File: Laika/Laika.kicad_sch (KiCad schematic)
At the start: 0 parts

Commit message: Defined Hierarchal Sheet Layout
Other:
- added sheet Project Architecture (sheets/ProjectArchitecture.kicad_sch)
- note added: "${BOARD_NAME}"
- note added: "${RELEASE_DATE}"
- note added: "1"
- note added: "10"
- note added: "11"
- note added: "12"
- note added: "13"
- note added: "14"
- note added: "15"
- note added: "2"
- note added: "3"
- note added: "4"
- note added: "5"
- note added: "6"
- note added: "7"
- note added: "8"
- note added: "9"
- note added: "Accelerometer"
- note added: "Barometer"
- note added: "Bottom"
- note added: "Cover Page"
- note added: "External Bus"
- note added: "GPS"
- note added: "IMU"
- note added: "Index"
- note added: "LoRa"
- note added: "Misc - Buttons and Buzzers"
- note added: "Notes"
- note added: "PWM and IO"
- note added: "Page"
- note added: "Power & Battery Management"
- note added: "Power Connectors"
- note added: "Project Architecture"
- note added: "Rev ${REVISION}"
- note added: "SD Card"
- note added: "Sensors"
- note added: "SoC"
- note added: "TOP"
- note added: "Variant: ${VARIANT}"
- company: (none) -> ${COMPANY}
- title: (none) -> ${BOARD_NAME}

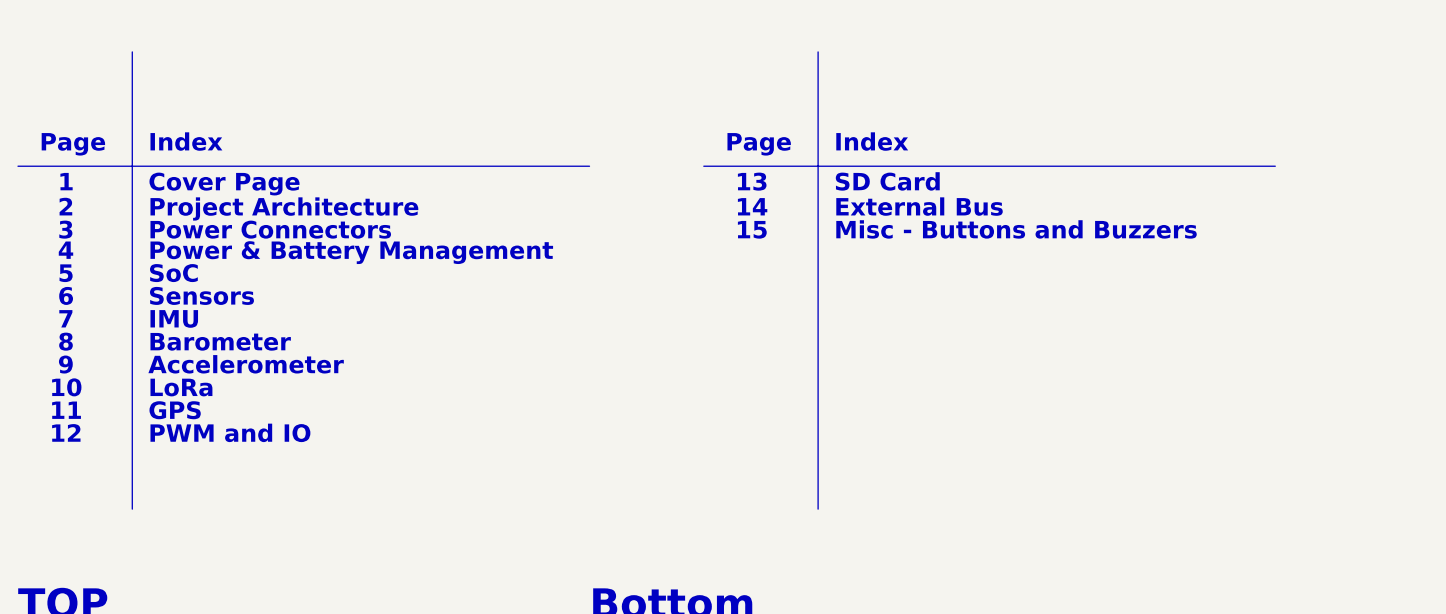
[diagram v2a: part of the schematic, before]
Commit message: Created Magnetometer Sheet
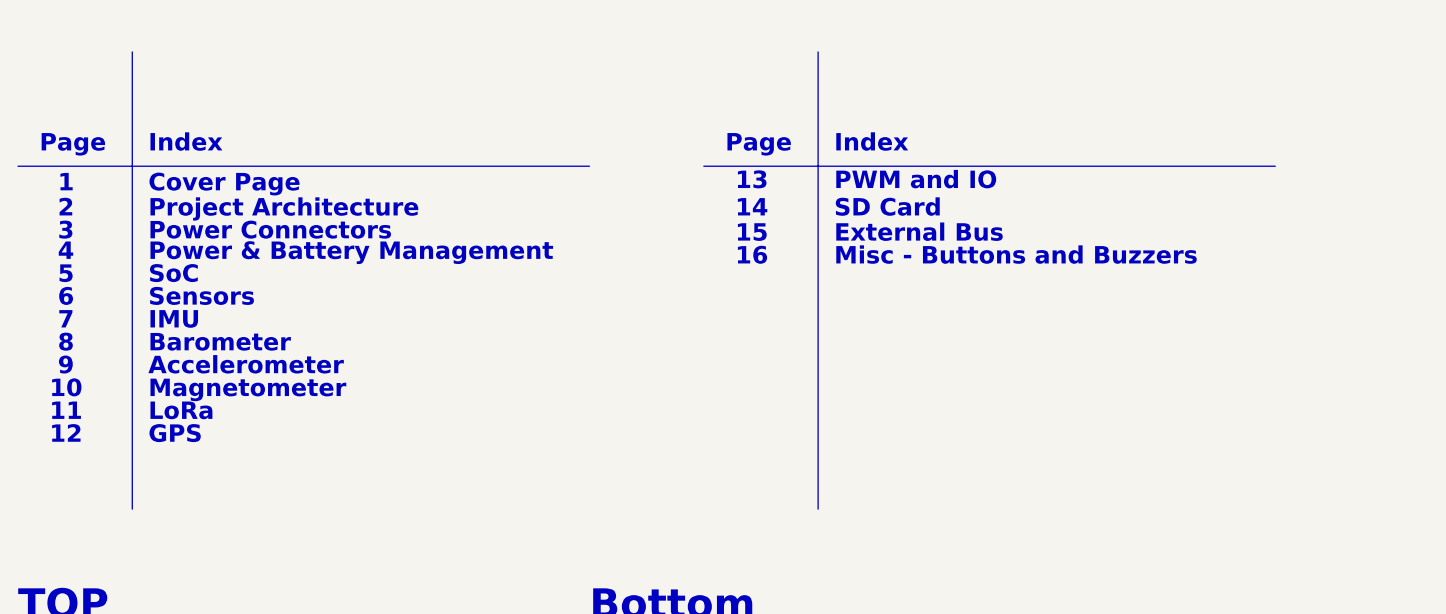
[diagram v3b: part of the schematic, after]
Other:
- note added: "16"
- note added: "Magnetometer"
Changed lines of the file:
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@@
 		)
 	)
-	(text "12"
-		(exclude_from_sim no)
-		(at 30.734 106.172 0)
+	(text "13"
+		(exclude_from_sim no)
+		(at 106.934 77.978 0)
 		(effects
 			(font
@@
 	(text "LoRa"
 		(exclude_from_sim no)
-		(at 39.878 101.092 0)
-		(effects
-			(font
-				(size 1.9304 1.9304)
-				(thickness 0.254)
-				(bold yes)
-			)
-			(justify left)
-			(href "#10")
+		(at 39.878 103.632 0)
+		(effects
+			(font
+				(size 1.9304 1.9304)
+				(thickness 0.254)
+				(bold yes)
+			)
+			(justify left)
+			(href "#11")
+		)
+	)
+	(text "15"
+		(exclude_from_sim no)
+		(at 106.934 83.82 0)
+		(effects
+			(font
+				(size 1.9304 1.9304)
+				(thickness 0.254)
+				(bold yes)
+				(color 0 0 0 1)
+			)
+		)
+	)
+	(text "PWM and IO"
+		(exclude_from_sim no)
+		(at 116.078 77.978 0)
+		(effects
+			(font
+				(size 1.9304 1.9304)
+				(thickness 0.254)
+				(bold yes)
+			)
+			(justify left)
+			(href "#13")
+		)
+	)
+	(text "Accelerometer"
+		(exclude_from_sim no)
+		(at 39.878 98.552 0)
+		(effects
+			(font
+				(size 1.9304 1.9304)
+				(thickness 0.254)
+				(bold yes)
+			)
+			(justify left)
+			(href "#9")
+		)
+	)
+	(text "7"
+		(exclude_from_sim no)
+		(at 30.734 93.472 0)
+		(effects
+			(font
+				(size 1.9304 1.9304)
+				(thickness 0.254)
+				(bold yes)
+				(color 0 0 0 1)
+			)
+		)
+	)
+	(text "IMU"
+		(exclude_from_sim no)
+		(at 39.878 93.472 0)
+		(effects
+			(font
+				(size 1.9304 1.9304)
+				(thickness 0.254)
+				(bold yes)
+			)
+			(justify left)
+			(href "#7")
+		)
+	)
+	(text "Cover Page"
+		(exclude_from_sim no)
+		(at 39.878 78.232 0)
+		(effects
+			(font
+				(size 1.9304 1.9304)
+				(thickness 0.254)
+				(bold yes)
+			)
+			(justify left)
+			(href "#1")
+		)
+	)
+	(text "10"
+		(exclude_from_sim no)
+		(at 30.734 101.092 0)
+		(effects
+			(font
+				(size 1.9304 1.9304)
+				(thickness 0.254)
+				(bold yes)
+				(color 0 0 0 1)
+			)
 		)
 	)
@@
 		)
 	)
-	(text "PWM and IO"
+	(text "6"
+		(exclude_from_sim no)
+		(at 30.734 90.932 0)
+		(effects
+			(font
+				(size 1.9304 1.9304)
+				(thickness 0.254)
+				(bold yes)
+				(color 0 0 0 1)
+			)
+		)
+	)
+	(text "GPS"
 		(exclude_from_sim no)
 		(at 39.878 106.172 0)
@@
 		)
 	)
-	(text "Accelerometer"
-		(exclude_from_sim no)
-		(at 39.878 98.552 0)
-		(effects
-			(font
-				(size 1.9304 1.9304)
-				(thickness 0.254)
-				(bold yes)
-			)
-			(justify left)
-			(href "#9")
-		)
-	)
-	(text "7"
-		(exclude_from_sim no)
-		(at 30.734 93.472 0)
-		(effects
-			(font
-				(size 1.9304 1.9304)
-				(thickness 0.254)
-				(bold yes)
-				(color 0 0 0 1)
-			)
-		)
-	)
-	(text "IMU"
-		(exclude_from_sim no)
-		(at 39.878 93.472 0)
-		(effects
-			(font
-				(size 1.9304 1.9304)
-				(thickness 0.254)
-				(bold yes)
-			)
-			(justify left)
-			(href "#7")
-		)
-	)
-	(text "Cover Page"
-		(exclude_from_sim no)
-		(at 39.878 78.232 0)
-		(effects
-			(font
-				(size 1.9304 1.9304)
-				(thickness 0.254)
-				(bold yes)
-			)
-			(justify left)
-			(href "#1")
-		)
-	)
-	(text "13"
-		(exclude_from_sim no)
-		(at 106.934 78.232 0)
-		(effects
-			(font
-				(size 1.9304 1.9304)
-				(thickness 0.254)
-				(bold yes)
-				(color 0 0 0 1)
-			)
-		)
-	)
-	(text "6"
-		(exclude_from_sim no)
-		(at 30.734 90.932 0)
-		(effects
-			(font
-				(size 1.9304 1.9304)
-				(thickness 0.254)
-				(bold yes)
-				(color 0 0 0 1)
-			)
-		)
-	)
-	(text "GPS"
-		(exclude_from_sim no)
-		(at 39.878 103.632 0)
-		(effects
-			(font
-				(size 1.9304 1.9304)
-				(thickness 0.254)
-				(bold yes)
-			)
-			(justify left)
-			(href "#11")
-		)
-	)
 	(text "Notes"
 		(exclude_from_sim no)
@@
 	(text "External Bus"
 		(exclude_from_sim no)
-		(at 116.078 81.026 0)
-		(effects
-			(font
-				(size 1.9304 1.9304)
-				(thickness 0.254)
-				(bold yes)
-			)
-			(justify left)
-			(href "#14")
+		(at 116.078 83.82 0)
+		(effects
+			(font
+				(size 1.9304 1.9304)
+				(thickness 0.254)
+				(bold yes)
+			)
+			(justify left)
+			(href "#15")
 		)
 	)
@@
 		)
 	)
-	(text "11"
-		(exclude_from_sim no)
-		(at 30.734 103.632 0)
+	(text "12"
+		(exclude_from_sim no)
+		(at 30.734 106.172 0)
 		(effects
 			(font
@@
 	(text "Misc - Buttons and Buzzers"
 		(exclude_from_sim no)
-		(at 116.078 83.566 0)
-		(effects
-			(font
-				(size 1.9304 1.9304)
-				(thickness 0.254)
-				(bold yes)
-			)
-			(justify left)
-			(href "#15")
+		(at 116.078 86.36 0)
+		(effects
+			(font
+				(size 1.9304 1.9304)
+				(thickness 0.254)
+				(bold yes)
+			)
+			(justify left)
+			(href "#16")
 		)
 	)
@@
 	(text "SD Card"
 		(exclude_from_sim no)
-		(at 116.078 78.232 0)
-		(effects
-			(font
-				(size 1.9304 1.9304)
-				(thickness 0.254)
-				(bold yes)
-			)
-			(justify left)
-			(href "#13")
-		)
-	)
-	(text "15"
-		(exclude_from_sim no)
-		(at 106.934 83.566 0)
+		(at 116.078 81.026 0)
+		(effects
+			(font
+				(size 1.9304 1.9304)
+				(thickness 0.254)
+				(bold yes)
+			)
+			(justify left)
+			(href "#14")
+		)
+	)
+	(text "16"
+		(exclude_from_sim no)
+		(at 106.934 86.36 0)
 		(effects
 			(font
@@
 		)
 	)
-	(text "10"
-		(exclude_from_sim no)
-		(at 30.734 101.092 0)
+	(text "11"
+		(exclude_from_sim no)
+		(at 30.734 103.632 0)
 		(effects
 			(font
@@
 		)
 	)
+	(text "Magnetometer"
+		(exclude_from_sim no)
+		(at 39.878 101.092 0)
+		(effects
+			(font
+				(size 1.9304 1.9304)
+				(thickness 0.254)
+				(bold yes)
+			)
+			(justify left)
+			(href "#10")
+		)
+	)
